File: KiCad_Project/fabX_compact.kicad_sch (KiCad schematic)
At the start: 62 parts, among them J1 Conn_02x15_Odd_Even, J2 Screw_Terminal_01x08, J3 Conn_02x07_Odd_Even, J4 Conn_01x06, J5 Conn_01x08, J6 Conn_01x08, K1 PLATZHALTER, Q1 2N7002, Q2 AO3401A, Q3 2N7002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

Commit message: some PCB progress
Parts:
- removed J5: Conn_01x08, Connector_PinSocket_2.54mm:PinSocket_2x05_P2.54mm_Vertical, symbol m5stackoutput_v2-rescue:Conn_01x10-Connector_Generic
- removed JP4, JP5, JP6: SolderJumper_3_Open, Jumper:SolderJumper-3_P1.3mm_Open_Pad1.0x1.5mm_NumberLabels, symbol m5stackoutput_v2-rescue:SolderJumper_3_Open-Jumper
- removed K1: PLATZHALTER, symbol Relay:FINDER-32.21-x300
- added J5: Conn_02x07_Odd_Even, Connector_IDC:IDC-Header_2x07_P2.54mm_Horizontal, symbol Connector_Generic:Conn_02x07_Odd_Even
- added JP4, JP5, JP6: SolderJumper_2_Open, Jumper:SolderJumper-2_P1.3mm_Open_RoundedPad1.0x1.5mm, symbol Jumper:SolderJumper_2_Open
- added K2: FINDER-36.11-4301, Relay_THT:Relay_SPST_TE_PCN-1xxD3MHZ, symbol Relay:FINDER-36.11-4301
- added R22, R23, R24: 10k, Resistor_SMD:R_0603_1608Metric, symbol Device:R
- C2: value C -> 100n 6v3 X7R
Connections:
- net 5V is gone; now on net +3V3: C2.2, U2.20 (Vdd), U2.6 (Reset)
- net +3V3: now also J5.1 (Pin_1), J5.2 (Pin_2), R22.1, R23.1, R24.1
- net +5V: now also J5.3 (Pin_3), J5.4 (Pin_4), K2.A1
- net Ch0: now also J3.14 (Pin_14); no longer J3.7 (Pin_7)
- net Ch1: now also J3.13 (Pin_13); no longer J3.8 (Pin_8)
- net Ch2: now also J3.12 (Pin_12); no longer J3.9 (Pin_9)
- net Ch3: now also J3.11 (Pin_11); no longer J3.10 (Pin_10)
- net Ch4: now also J3.10 (Pin_10); no longer J3.11 (Pin_11)
- net Ch5: now also J3.9 (Pin_9); no longer J3.12 (Pin_12)
- net Ch6: now also J3.8 (Pin_8); no longer J3.13 (Pin_13)
- net Ch7: now also J3.7 (Pin_7); no longer J3.14 (Pin_14)
- net Fet0: now also K2.A2
- net GND: now also J5.5 (Pin_5), J5.6 (Pin_6), JP4.1 (A), JP5.1 (A), JP6.1 (A)
- net NFC_CS: now also J1.19 (Pin_19); no longer J1.10 (Pin_10)
- net NFC_IRQ: now also J1.10 (Pin_10); no longer J1.20 (Pin_20)
- net NFC_RST: now also J1.20 (Pin_20); no longer J1.19 (Pin_19)
- net Relay_COM: now also K2.11
- net Relay_NO: now also K2.14
- net Ch17: now reaches U2.19 (GP7)
- net Ch17: now also J5.7 (Pin_7)
- net at U2.3 (A2): now also JP6.2 (B), R24.2
- net at U2.4 (A1): now also JP5.2 (B), R23.2
- net at U2.5 (A0): now also JP4.2 (B), R22.2
- net In1 renamed Ch10
- net Ch10: now also J5.14 (Pin_14)
- net In2 renamed Ch11
- net Ch11: now also J5.13 (Pin_13)
- net In3 renamed Ch12
- net Ch12: now also J5.12 (Pin_12)
- net In4 renamed Ch13
- net Ch13: now also J5.11 (Pin_11)
- net In5 renamed Ch14
- net Ch14: now also J5.10 (Pin_10)
- net In6 renamed Ch15
- net Ch15: now also J5.9 (Pin_9)
- net In7 renamed Ch16
- net Ch16: now also J5.8 (Pin_8)
- no-connect marks 14 -> 15
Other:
- note added: "Input Expander Da lassen? Ist auch noch flasch mit 5V versorgt 3V3 ist richtig!"
- note added: "Inputs Da lassen Flachband expansion"
- note removed: "Hier war ein Dreher drin wenn ich das richtig in Erinnerung habe? passt eignetlich zu dem hier oder? https://www.amazon.de/Cylewet-FT232RL-Adapter-Arduino-Interface/dp/B01MU5E31B"
- note removed: "I2C Port Expander 8 Bit each"
- note removed: "Input Expander Da lassen? Ist auch noch flasch mit 5V versorgt"
- note removed: "mapped to random GPIO. Any special Function neccesary?"

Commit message: PCB progress
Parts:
- removed H1, H2: MountingHole_Pad, TestPoint:TestPoint_Loop_D2.50mm_Drill1.85mm, symbol m5stackoutput_v2-rescue:MountingHole_Pad-Mechanical
- C1, C2: Farnell# (none) -> 3345771; Mnf (none) -> Vishay; Mnf# (none) -> VJ0603Y104KXXPW1BC
- D1: footprint Diode_SMD:D_SOD-123 -> Diode_SMD:D_; Farnell# (none) -> 2760409; Mnf (none) -> Nexperia; Mnf# (none) -> PMEG3020EGWX
- D2, D3, D4, D5: footprint LED_SMD:LED_0603_1608Metric -> LED_SMD:LED_1206_3216Metric_ReverseMount_Hole1.8x2.4mm; Farnell# (none) -> 2099257; Mnf (none) -> Kingbright; Mnf# (none) -> KPTR-3216SYCK
- H10, H12, H13, H4, H6, H7: footprint MountingHole:MountingHole_3.2mm_M3 -> ownCon:MountingHole_3.2mm_M3_noSolder; Farnell# (none) -> -; Mnf (none) -> -; Mnf# (none) -> -
- H11, H5, H8, H9: footprint MountingHole:MountingHole_3.2mm_M3 -> ownCon:MountingHole_3.2mm_M3_noSolderCorner; Farnell# (none) -> -; Mnf (none) -> -; Mnf# (none) -> -
- H3, R15: Farnell# (none) -> -; Mnf (none) -> -; Mnf# (none) -> -
- J1: renamed from JP1; Farnell# (none) -> -; Mnf (none) -> -; Mnf# (none) -> -
- J2: renamed from JP2; Farnell# (none) -> -; Mnf (none) -> -; Mnf# (none) -> -
- J3: renamed from JP3; Farnell# (none) -> -; Mnf (none) -> -; Mnf# (none) -> -
- J4: renamed from JP4; Farnell# (none) -> -; Mnf (none) -> -; Mnf# (none) -> -
- J5: renamed from JP5; Farnell# (none) -> -; Mnf (none) -> -; Mnf# (none) -> -
- J6: renamed from JP6; Farnell# (none) -> -; Mnf (none) -> -; Mnf# (none) -> -
- K2: value FINDER-36.11-4301 -> PCN-105D3MHZ; symbol Relay:FINDER-36.11-4301 -> Relay:UMS05-1A80-75L; Farnell# (none) -> 4444930; Mnf (none) -> TE; Mnf# (none) -> PCN-105D3MHZ
- Q1, Q3, Q4: Farnell# (none) -> 3924478; Mnf (none) -> Nexperia; Mnf# (none) -> 2N7002HR
- Q2: value AO3401A -> DMP3056L-7; Farnell# (none) -> 3127362; Mnf (none) -> Diodes; Mnf# (none) -> DMP3056L-7
- Q5, Q6: Farnell# (none) -> 2317581; Mnf (none) -> onsemi; Mnf# (none) -> BCX19LT1G
- R1, R8: Farnell# (none) -> 3495222; Mnf (none) -> Yageo; Mnf# (none) -> AC0603FR-07100KL
- R10, R12, R13, R9: Farnell# (none) -> 3495238; Mnf (none) -> Yageo; Mnf# (none) -> AC0603FR-071KL
- R11, R2, R20, R21, R22, R23, R24, R3, R4, R5, R6, R7: Farnell# (none) -> 3495224; Mnf (none) -> Yageo; Mnf# (none) -> AC0603FR-0710KL
- R14: Farnell# (none) -> 2309106; Mnf (none) -> Yageo; Mnf# (none) -> RC0603FR-070RL
- R16, R19: footprint Resistor_SMD:R_0603_1608Metric -> Resistor_SMD:R_2010_5025Metric; Farnell# (none) -> -; Mnf (none) -> -; Mnf# (none) -> -
- R17, R18: Farnell# (none) -> 3950907; Mnf (none) -> Yageo; Mnf# (none) -> AC0603FR-07330RL
- U1, U2: Farnell# (none) -> 1605564; Mnf (none) -> Microchip; Mnf# (none) -> MCP23008-E/SS
- X1: renamed from J1; Farnell# (none) -> -; Mnf (none) -> MISC/VORRAT; Mnf# (none) -> testen mit Prototyp wegen höhe
- X2: renamed from J2; footprint (none) -> Connector_Phoenix_MSTB:PhoenixContact_MSTBA_2,5_8-G-5,08_1x08_P5.08mm_Horizontal; Farnell# (none) -> 2671266; Mnf (none) -> Phoenix; Mnf# (none) -> MSTB 2,5/ 8-G-5,08
- X3: renamed from J3; Farnell# (none) -> 2356264; Mnf (none) -> Wuerth; Mnf# (none) -> 61201421721
- X4: renamed from J4; Farnell# (none) -> 2084276; Mnf (none) -> GCT; Mnf# (none) -> BG302-06-A-L-G
- X5: renamed from J5; Farnell# (none) -> 2356264; Mnf (none) -> Wuerth; Mnf# (none) -> 61201421721
- X6: renamed from J6; Farnell# (none) -> -; Mnf (none) -> MISC/VORRAT; Mnf# (none) -> testen mit Prototyp wegen höhe
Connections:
- net 3,3V is gone; now on net +3V3: X4.3 (Pin_3)
- net +5V: now also K2.2; no longer K2.A1
- net Fet0: now also K2.1; no longer K2.A2
- net Relay_COM: now also K2.3; no longer K2.11
- net Relay_NO: now also K2.4; no longer K2.14
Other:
- note removed: "Add soem C on 5V/3V3"
- note removed: "Input Expander Da lassen? Ist auch noch flasch mit 5V versorgt 3V3 ist richtig!"
- note removed: "Inputs Da lassen Flachband expansion"
- note removed: "PWR"
- moved on the sheet: C1, C2, D2, D3, D4, D5, H10, H11, H12, H13, H4, H6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

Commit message: added bom
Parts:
- D2, D3, D4, D5: footprint LED_SMD:LED_1206_3216Metric_ReverseMount_Hole1.8x2.4mm -> ownLEDs:LED_1206_3216Metric_ReverseMount_Hole1.8x2.4mm_3DMOD
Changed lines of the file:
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@@
     (property "Reference" "D2" (id 0) (at 53.34 156.21 0))
     (property "Value" "LED" (id 1) (at 53.34 161.29 0))
-    (property "Footprint" "LED_SMD:LED_1206_3216Metric_ReverseMount_Hole1.8x2.4mm" (id 2) (at 53.34 158.75 0)
+    (property "Footprint" "ownLEDs:LED_1206_3216Metric_ReverseMount_Hole1.8x2.4mm_3DMOD" (id 2) (at 53.34 158.75 0)
       (effects (font (size 1.27 1.27)) hide)
     )
@@
     (property "Reference" "D4" (id 0) (at 53.34 171.45 0))
     (property "Value" "LED" (id 1) (at 53.34 176.53 0))
-    (property "Footprint" "LED_SMD:LED_1206_3216Metric_ReverseMount_Hole1.8x2.4mm" (id 2) (at 53.34 173.99 0)
+    (property "Footprint" "ownLEDs:LED_1206_3216Metric_ReverseMount_Hole1.8x2.4mm_3DMOD" (id 2) (at 53.34 173.99 0)
       (effects (font (size 1.27 1.27)) hide)
     )
@@
     (property "Reference" "D3" (id 0) (at 53.34 163.83 0))
     (property "Value" "LED" (id 1) (at 53.34 168.91 0))
-    (property "Footprint" "LED_SMD:LED_1206_3216Metric_ReverseMount_Hole1.8x2.4mm" (id 2) (at 53.34 166.37 0)
+    (property "Footprint" "ownLEDs:LED_1206_3216Metric_ReverseMount_Hole1.8x2.4mm_3DMOD" (id 2) (at 53.34 166.37 0)
       (effects (font (size 1.27 1.27)) hide)
     )
@@
     (property "Reference" "D5" (id 0) (at 53.34 182.88 0))
     (property "Value" "LED" (id 1) (at 53.34 187.96 0))
-    (property "Footprint" "LED_SMD:LED_1206_3216Metric_ReverseMount_Hole1.8x2.4mm" (id 2) (at 53.34 185.42 0)
+    (property "Footprint" "ownLEDs:LED_1206_3216Metric_ReverseMount_Hole1.8x2.4mm_3DMOD" (id 2) (at 53.34 185.42 0)
       (effects (font (size 1.27 1.27)) hide)
     )
@@
     )
     (path "/179e501c-461c-406b-aafa-61f5dcc1e5c0"
-      (reference "D2") (unit 1) (value "LED") (footprint "LED_SMD:LED_1206_3216Metric_ReverseMount_Hole1.8x2.4mm")
+      (reference "D2") (unit 1) (value "LED") (footprint "ownLEDs:LED_1206_3216Metric_ReverseMount_Hole1.8x2.4mm_3DMOD")
     )
     (path "/95e89a79-f538-4bf5-a2d8-6c390213df34"
-      (reference "D3") (unit 1) (value "LED") (footprint "LED_SMD:LED_1206_3216Metric_ReverseMount_Hole1.8x2.4mm")
+      (reference "D3") (unit 1) (value "LED") (footprint "ownLEDs:LED_1206_3216Metric_ReverseMount_Hole1.8x2.4mm_3DMOD")
     )
     (path "/7c56ee33-0325-44ec-864b-328ff84f728a"
-      (reference "D4") (unit 1) (value "LED") (footprint "LED_SMD:LED_1206_3216Metric_ReverseMount_Hole1.8x2.4mm")
+      (reference "D4") (unit 1) (value "LED") (footprint "ownLEDs:LED_1206_3216Metric_ReverseMount_Hole1.8x2.4mm_3DMOD")
     )
     (path "/d936d692-b1d5-435c-a77f-1e1bd4cd670a"
-      (reference "D5") (unit 1) (value "LED") (footprint "LED_SMD:LED_1206_3216Metric_ReverseMount_Hole1.8x2.4mm")
+      (reference "D5") (unit 1) (value "LED") (footprint "ownLEDs:LED_1206_3216Metric_ReverseMount_Hole1.8x2.4mm_3DMOD")
     )
     (path "/b6879009-9ec5-4a01-8abe-cf757f8ef06c"

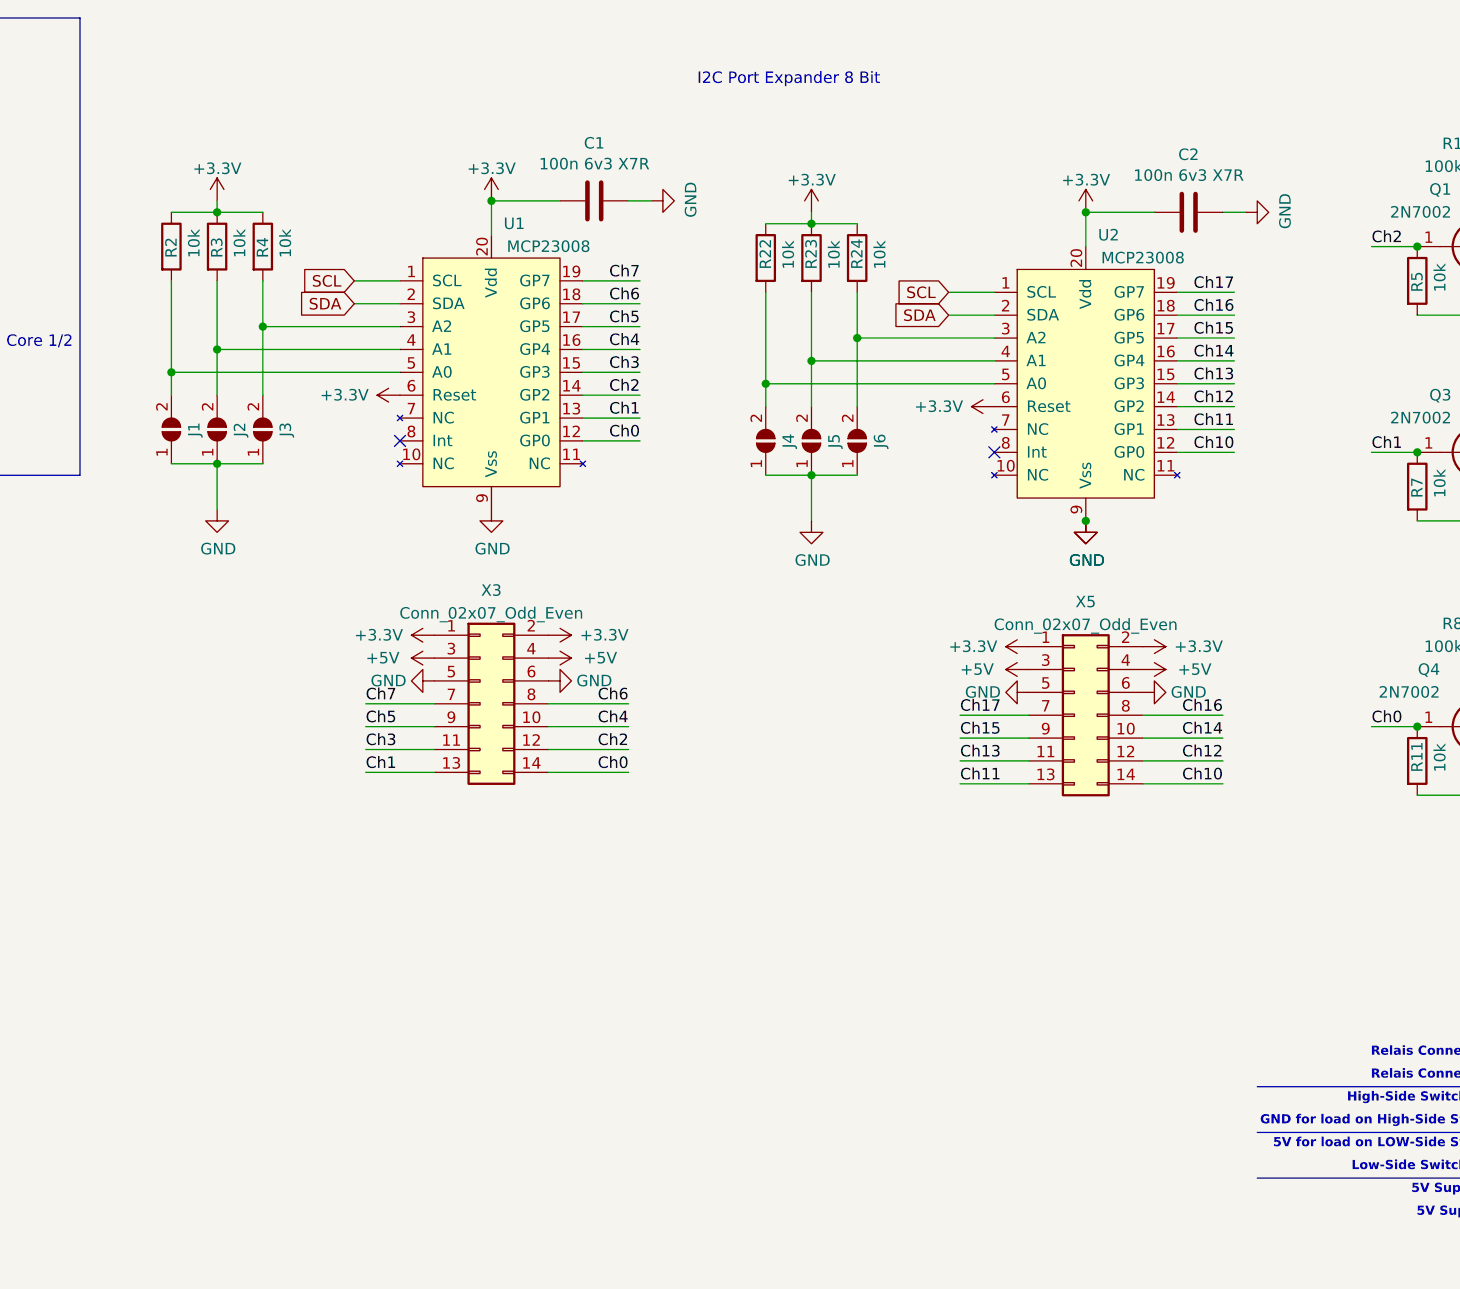
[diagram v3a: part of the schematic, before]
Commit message: add pulldowns for inputs
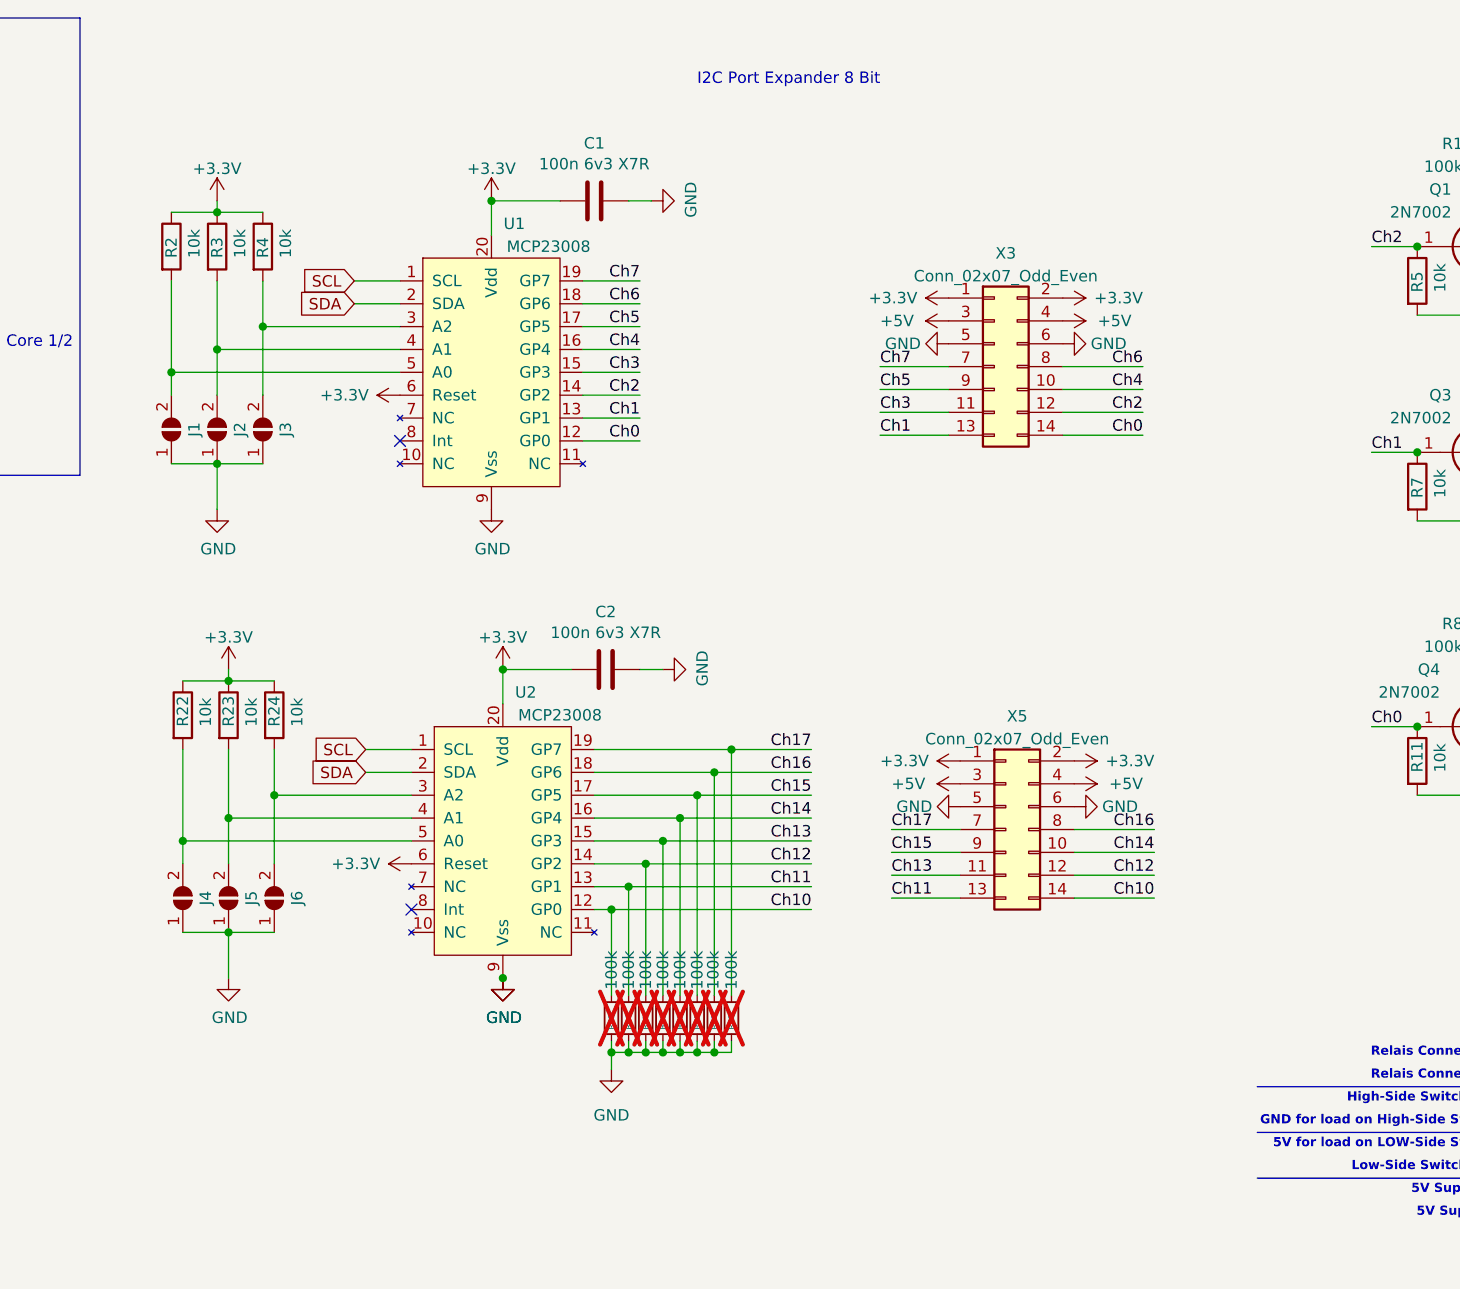
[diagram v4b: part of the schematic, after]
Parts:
- added R25, R26, R27, R28, R29, R30, R31, R32: 100k, symbol Device:R_Small
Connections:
- net Ch10: now also R25.1
- net Ch11: now also R26.1
- net Ch12: now also R27.1
- net Ch13: now also R28.1
- net Ch14: now also R29.1
- net Ch15: now also R30.1
- net Ch16: now also R31.1
- net Ch17: now also R32.1
- net GND: now also R25.2, R26.2, R27.2, R28.2, R29.2, R30.2, R31.2, R32.2
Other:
- moved on the sheet: C2, J4, J5, J6, R22, R23, R24, U2, X3, X5

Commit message: new PCB Version V0.2
Added new Pulddown Rs to PCB
DRC okay
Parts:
- R25, R26, R27, R28, R29, R30, R31, R32: footprint (none) -> Resistor_SMD:R_0603_1608Metric
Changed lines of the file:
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@@
       (effects (font (size 1.27 1.27)) (justify left))
     )
-    (property "Footprint" "" (at 157.48 126.365 0)
+    (property "Footprint" "Resistor_SMD:R_0603_1608Metric" (at 157.48 126.365 0)
       (effects (font (size 1.27 1.27)) hide)
     )
@@
       (effects (font (size 1.27 1.27)) hide)
     )
-    (pin "2")
-    (pin "1")
+    (pin "1")
+    (pin "2")
     (instances
       (project "fabX_compact"
@@
       (effects (font (size 1.27 1.27)) (justify left))
     )
-    (property "Footprint" "" (at 147.955 126.365 0)
+    (property "Footprint" "Resistor_SMD:R_0603_1608Metric" (at 147.955 126.365 0)
       (effects (font (size 1.27 1.27)) hide)
     )
@@
       (effects (font (size 1.27 1.27)) hide)
     )
-    (pin "2")
-    (pin "1")
+    (pin "1")
+    (pin "2")
     (instances
       (project "fabX_compact"
@@
       (effects (font (size 1.27 1.27)) (justify left))
     )
-    (property "Footprint" "" (at 146.05 126.365 0)
+    (property "Footprint" "Resistor_SMD:R_0603_1608Metric" (at 146.05 126.365 0)
       (effects (font (size 1.27 1.27)) hide)
     )
@@
       (effects (font (size 1.27 1.27)) hide)
     )
-    (pin "2")
-    (pin "1")
+    (pin "1")
+    (pin "2")
     (instances
       (project "fabX_compact"
@@
       (effects (font (size 1.27 1.27)) (justify left))
     )
-    (property "Footprint" "" (at 153.67 126.365 0)
+    (property "Footprint" "Resistor_SMD:R_0603_1608Metric" (at 153.67 126.365 0)
       (effects (font (size 1.27 1.27)) hide)
     )
@@
       (effects (font (size 1.27 1.27)) hide)
     )
-    (pin "2")
-    (pin "1")
+    (pin "1")
+    (pin "2")
     (instances
       (project "fabX_compact"
@@
       (effects (font (size 1.27 1.27)) (justify left))
     )
-    (property "Footprint" "" (at 155.575 126.365 0)
+    (property "Footprint" "Resistor_SMD:R_0603_1608Metric" (at 155.575 126.365 0)
       (effects (font (size 1.27 1.27)) hide)
     )
@@
       (effects (font (size 1.27 1.27)) hide)
     )
-    (pin "2")
-    (pin "1")
+    (pin "1")
+    (pin "2")
     (instances
       (project "fabX_compact"
@@
       (effects (font (size 1.27 1.27)) (justify left))
     )
-    (property "Footprint" "" (at 144.145 126.365 0)
+    (property "Footprint" "Resistor_SMD:R_0603_1608Metric" (at 144.145 126.365 0)
       (effects (font (size 1.27 1.27)) hide)
     )
@@
       (effects (font (size 1.27 1.27)) hide)
     )
-    (pin "2")
-    (pin "1")
+    (pin "1")
+    (pin "2")
     (instances
       (project "fabX_compact"
@@
       (effects (font (size 1.27 1.27)) (justify left))
     )
-    (property "Footprint" "" (at 151.765 126.365 0)
+    (property "Footprint" "Resistor_SMD:R_0603_1608Metric" (at 151.765 126.365 0)
       (effects (font (size 1.27 1.27)) hide)
     )
@@
       (effects (font (size 1.27 1.27)) hide)
     )
-    (pin "2")
-    (pin "1")
+    (pin "1")
+    (pin "2")
     (instances
       (project "fabX_compact"
@@
       (effects (font (size 1.27 1.27)) (justify left))
     )
-    (property "Footprint" "" (at 149.86 126.365 0)
+    (property "Footprint" "Resistor_SMD:R_0603_1608Metric" (at 149.86 126.365 0)
       (effects (font (size 1.27 1.27)) hide)
     )
@@
       (effects (font (size 1.27 1.27)) hide)
     )
-    (pin "2")
-    (pin "1")
-    (instances
-      (project "fabX_compact"
+    (pin "1")
+    (pin "2")
+    (instances
+      (project "fabX_compact"
